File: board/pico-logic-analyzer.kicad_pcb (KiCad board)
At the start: 4 copper layers, 85 x 57.5 mm, 67 parts, among them J1 Conn_02x03_Odd_Even, J10 Conn_02x03_Odd_Even, J11 Conn_01x01, J2 Conn_02x03_Odd_Even, J3 Conn_02x03_Odd_Even, J4 Conn_02x03_Odd_Even, J5 Conn_02x03_Odd_Even, J6 Conn_02x03_Odd_Even, J7 Conn_02x03_Odd_Even, J8 Conn_02x03_Odd_Even, J9 Conn_02x03_Odd_Even, SW1 SW_Push, SW2 SW_DIP_x04, SW3 SW_DIP_x04, SW4 SW_DIP_x04, U1 LM2665M6, U2 LM4040DBZ-5, U3 TXB0104PW (fit with U104), U4 TXB0104PW (fit with U104), U5 TXB0104PW (fit with U104)

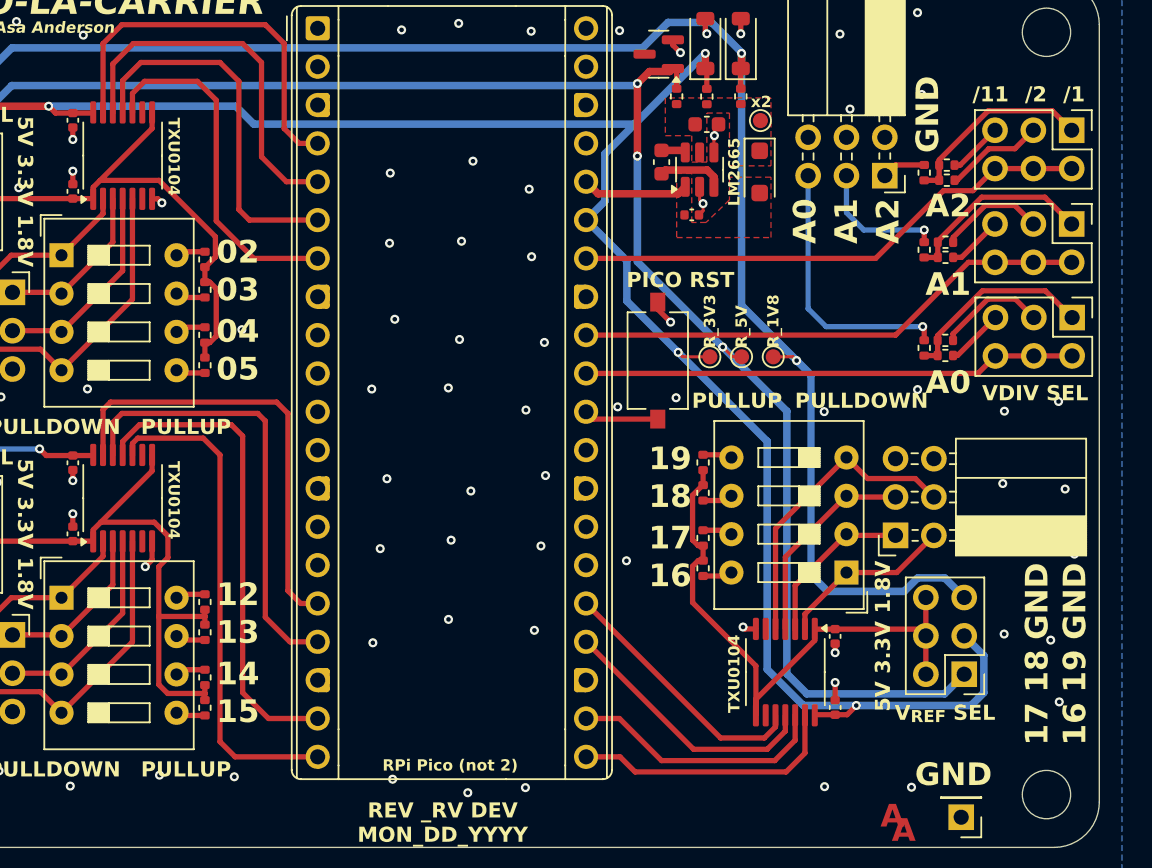
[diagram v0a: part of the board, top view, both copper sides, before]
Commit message: 2.0 first commit * started switching caps to standard value of 0603 4.7uF (which is overkill everywhere) * tidied up some silkscreen * replaced 4x100kOhm pullup resistors with 1 array (of the same values) * made some space for the zener clamping circuit (will still be a very tight fit)
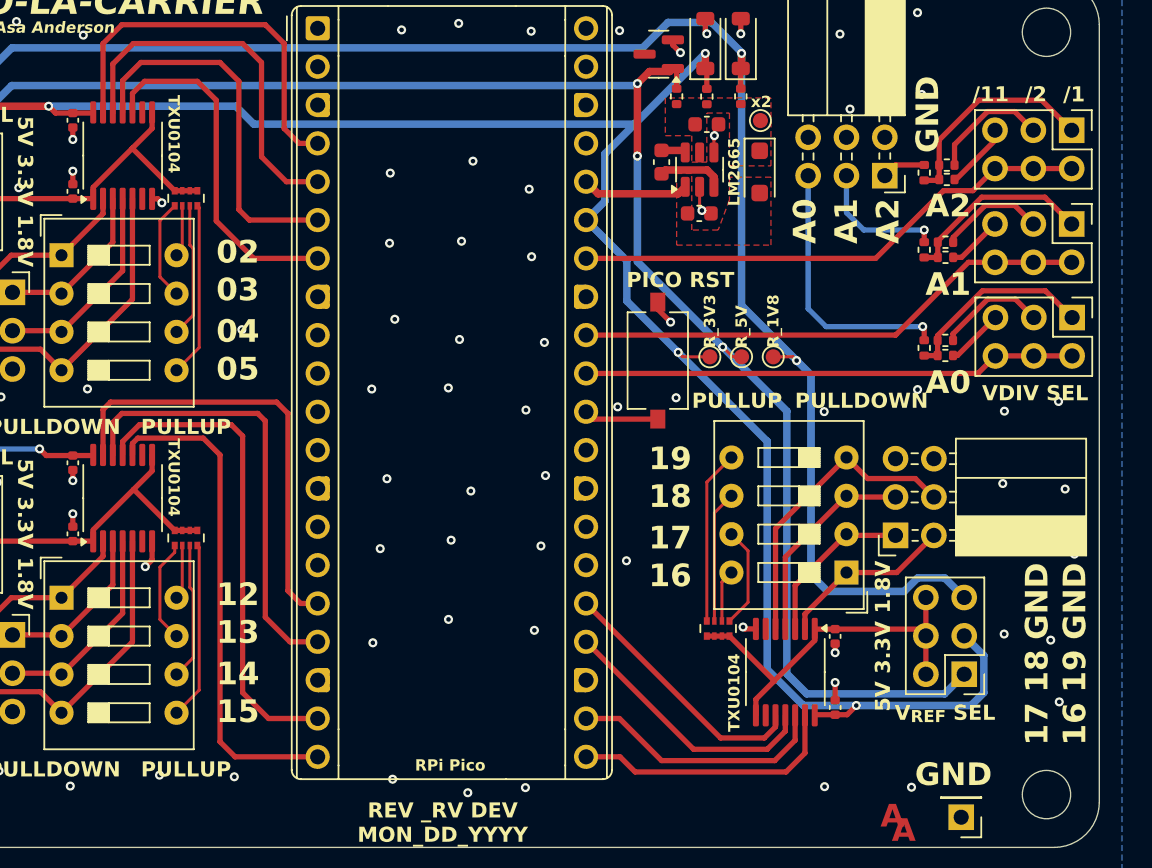
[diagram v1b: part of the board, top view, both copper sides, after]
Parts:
- removed R10, R11, R12, R13, R14, R15, R4, R5, R6, R7, R8, R9: 100k, Resistor_SMD:R_0402_1005Metric
- added RN1: 100k, Resistor_SMD:R_Array_Convex_4x0402, F.Cu at (150.5, 89.0)
- added RN2: 100k, Resistor_SMD:R_Array_Convex_4x0402, F.Cu at (150.5, 66.5)
- added RN3: 100k, Resistor_SMD:R_Array_Convex_4x0402, F.Cu at (185.8, 95.0)
- C1: value 1 uF -> 4.7 uF; footprint Capacitor_SMD:C_0402_1005Metric -> Capacitor_SMD:C_0603_1608Metric
- moved R17 1.00 mm to (200.9, 64.3)
- moved R18 0.95 mm to (200.9, 65.2)
- moved C1 0.51 mm to (184.5, 67.5)
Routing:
- net /Buffer Block A/VCCA_SEL: track 42.6 -> 24.7 mm
- net /Buffer Block C/VCCA_SEL: track 38.5 -> 25.0 mm
- net /Buffer Block B/VCCA_SEL: track 37.8 -> 24.8 mm
- net Net-(RN1D-R4.1): track 1.70 -> 11.8 mm
- net Net-(RN2D-R4.1): track 1.70 -> 11.6 mm
- net Net-(RN3D-R4.1): track 1.70 -> 11.5 mm
- net Net-(RN1C-R3.1): track 1.57 -> 9.09 mm
- net Net-(RN2C-R3.1): track 1.57 -> 8.90 mm
- net Net-(RN3C-R3.1): track 1.57 -> 8.76 mm
- net Net-(RN1A-R1.1): track 1.62 -> 6.86 mm
- net Net-(RN3A-R1.1): track 1.62 -> 6.72 mm
- net Net-(RN2A-R1.1): track 1.62 -> 6.67 mm
- net Net-(RN1B-R2.1): track 1.65 -> 3.62 mm
- net Net-(RN3B-R2.1): track 1.65 -> 3.47 mm
- net Net-(RN2B-R2.1): track 1.65 -> 3.43 mm
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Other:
- board text added: "RPi Pico"
- board text removed: "RPi Pico (not 2)"

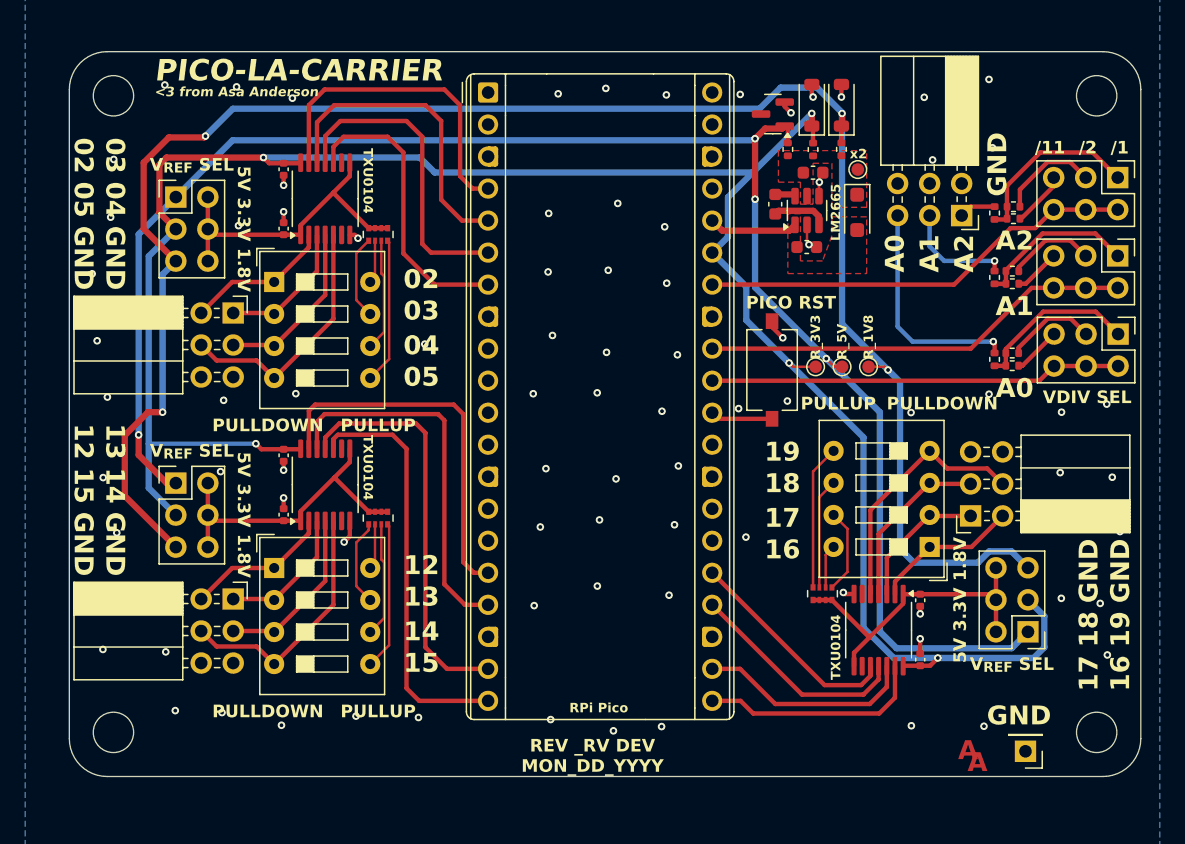
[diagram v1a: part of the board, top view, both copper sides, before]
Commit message: add zener diode clamping circuit
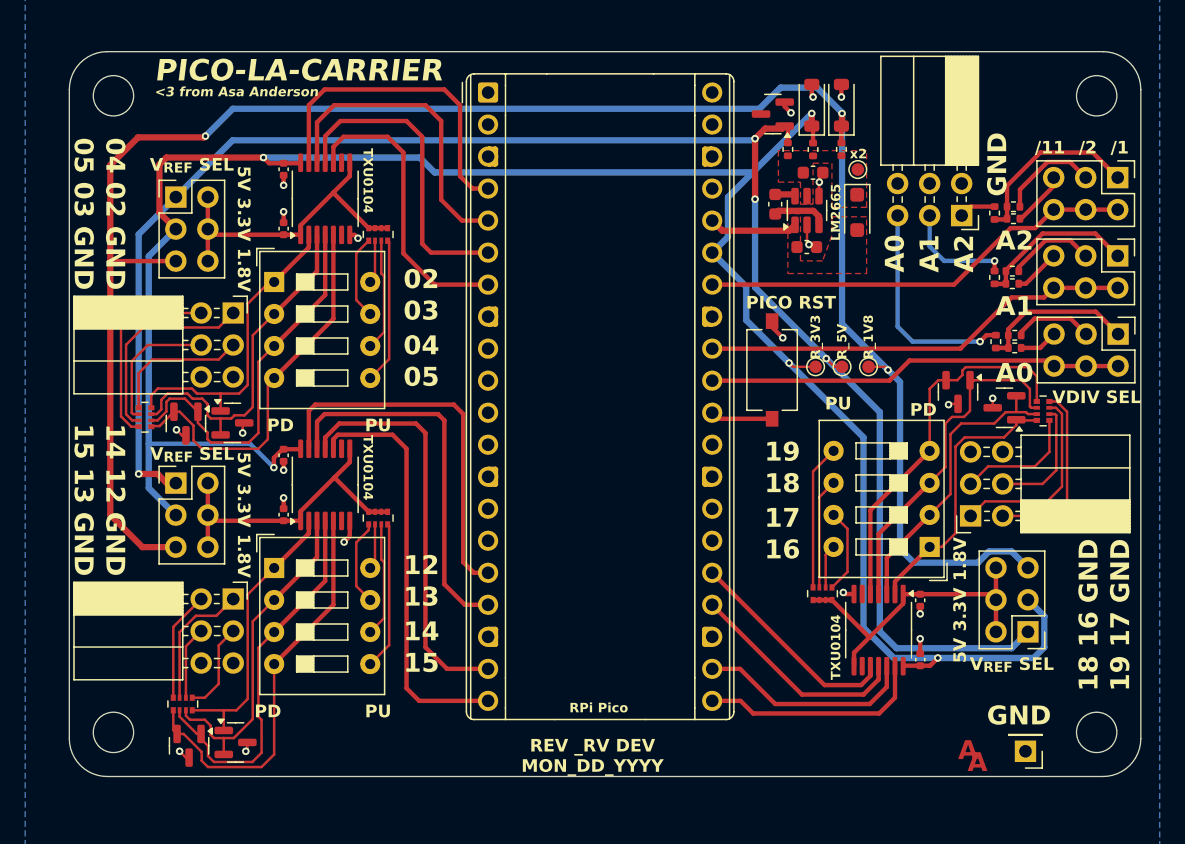
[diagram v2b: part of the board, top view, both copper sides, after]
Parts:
- added D4: 6.2 V_{z}, prefer better tolerances, Package_TO_SOT_SMD:SOT-23, F.Cu at (135.5, 107.1)
- added D5: 6.2 V_{z}, prefer better tolerances, Package_TO_SOT_SMD:SOT-23, F.Cu at (135.2, 81.5)
- added D6: 6.2 V_{z}, prefer better tolerances, Package_TO_SOT_SMD:SOT-23, F.Cu at (196.5, 79.0)
- added D7: 6.2 V_{z}, prefer better tolerances, Package_TO_SOT_SMD:SOT-23, F.Cu at (139.2, 106.8)
- added D8: 6.2 V_{z}, prefer better tolerances, Package_TO_SOT_SMD:SOT-23, F.Cu at (138.9, 81.5)
- added D9: 6.2 V_{z}, prefer better tolerances, Package_TO_SOT_SMD:SOT-23, F.Cu at (200.2, 80.2)
- added RN4: 470, Resistor_SMD:R_Array_Convex_4x0402, F.Cu at (135.0, 103.8)
- added RN5: 470, Resistor_SMD:R_Array_Convex_4x0402, F.Cu at (132.0, 81.0)
- added RN6: 470, Resistor_SMD:R_Array_Convex_4x0402, F.Cu at (203.2, 80.5)
- moved R23 1.42 mm to (201.0, 74.5)
- moved R24 1.42 mm to (201.0, 75.5)
- moved R22 1.41 mm to (199.5, 75.0)
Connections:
- J3 pad 1: /Buffer Block A/A1 -> /Buffer Block A/A2
- J3 pad 2: /Buffer Block A/A0 -> /Buffer Block A/A3
- J3 pad 3: /Buffer Block A/A2 -> /Buffer Block A/A0
- J3 pad 4: /Buffer Block A/A3 -> /Buffer Block A/A1
- J5 pad 1: /Buffer Block B/A1 -> /Buffer Block B/A2
- J5 pad 2: /Buffer Block B/A0 -> /Buffer Block B/A3
- J5 pad 3: /Buffer Block B/A2 -> /Buffer Block B/A0
- J5 pad 4: /Buffer Block B/A3 -> /Buffer Block B/A1
- J7 pad 1: /Buffer Block C/A1 -> /Buffer Block C/A2
- J7 pad 2: /Buffer Block C/A0 -> /Buffer Block C/A3
- J7 pad 3: /Buffer Block C/A2 -> /Buffer Block C/A0
- J7 pad 4: /Buffer Block C/A3 -> /Buffer Block C/A1
- SW2 pad 1: /Buffer Block A/A0 -> /Buffer Block A/A0_{CL}
- SW2 pad 2: /Buffer Block A/A1 -> /Buffer Block A/A1_{CL}
- SW2 pad 3: /Buffer Block A/A2 -> /Buffer Block A/A2_{CL}
- SW2 pad 4: /Buffer Block A/A3 -> /Buffer Block A/A3_{CL}
- SW3 pad 1: /Buffer Block B/A0 -> /Buffer Block B/A0_{CL}
- SW3 pad 2: /Buffer Block B/A1 -> /Buffer Block B/A1_{CL}
- SW3 pad 3: /Buffer Block B/A2 -> /Buffer Block B/A2_{CL}
- SW3 pad 4: /Buffer Block B/A3 -> /Buffer Block B/A3_{CL}
- SW4 pad 1: /Buffer Block C/A0 -> /Buffer Block C/A0_{CL}
- SW4 pad 2: /Buffer Block C/A1 -> /Buffer Block C/A1_{CL}
- SW4 pad 3: /Buffer Block C/A2 -> /Buffer Block C/A2_{CL}
- SW4 pad 4: /Buffer Block C/A3 -> /Buffer Block C/A3_{CL}
- U3 pad 2: /Buffer Block A/A0 -> /Buffer Block A/A0_{CL}
- U3 pad 3: /Buffer Block A/A1 -> /Buffer Block A/A1_{CL}
- U3 pad 4: /Buffer Block A/A2 -> /Buffer Block A/A2_{CL}
- U3 pad 5: /Buffer Block A/A3 -> /Buffer Block A/A3_{CL}
- U4 pad 2: /Buffer Block B/A0 -> /Buffer Block B/A0_{CL}
- U4 pad 3: /Buffer Block B/A1 -> /Buffer Block B/A1_{CL}
- U4 pad 4: /Buffer Block B/A2 -> /Buffer Block B/A2_{CL}
- U4 pad 5: /Buffer Block B/A3 -> /Buffer Block B/A3_{CL}
- U5 pad 2: /Buffer Block C/A0 -> /Buffer Block C/A0_{CL}
- U5 pad 3: /Buffer Block C/A1 -> /Buffer Block C/A1_{CL}
- U5 pad 4: /Buffer Block C/A2 -> /Buffer Block C/A2_{CL}
- U5 pad 5: /Buffer Block C/A3 -> /Buffer Block C/A3_{CL}
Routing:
- net /Buffer Block A/A3_{CL}: track 0.00 -> 32.1 mm
- net /Buffer Block B/A3_{CL}: track 0.00 -> 30.3 mm
- net /Buffer Block B/A2_{CL}: track 0.00 -> 30.2 mm
- net /Buffer Block C/A3_{CL}: track 0.00 -> 30.0 mm
- net /Buffer Block A/A2_{CL}: track 0.00 -> 29.8 mm
- net /Buffer Block B/A1_{CL}: track 0.00 -> 28.0 mm
- net /Buffer Block C/A2_{CL}: track 0.00 -> 27.7 mm
- net /Buffer Block A/A1_{CL}: track 0.00 -> 26.7 mm
- net /Buffer Block B/A0_{CL}: track 0.00 -> 24.5 mm
- net /Buffer Block C/A1_{CL}: track 0.00 -> 23.6 mm
- net /Buffer Block A/A0_{CL}: track 0.00 -> 22.5 mm
- net /Buffer Block C/A0_{CL}: track 0.00 -> 21.8 mm
- net /Buffer Block A/A3: track 20.2 -> 8.75 mm
- net /+1.8V_REG: track 146.2 -> 152.7 mm, vias 4 -> 3
- net /Buffer Block C/A3: track 20.2 -> 14.4 mm
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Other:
- board text added: "PD"
- board text added: "PU"
- board text removed: "PULLDOWN"
- board text removed: "PULLUP"

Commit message: remove 3.3v zener from sch - start to switch to stdlib rpi pico -
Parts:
- removed D3: 3.3v, Diode_SMD:D_SOD-123
- removed R2: 270, >1/10 W, Resistor_SMD:R_0402_1005Metric
- removed TP1, TP2, TP3: TestPoint, TestPoint:TestPoint_Pad_D1.0mm
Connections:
- A1 pad 35: /+3.3V_REG -> unconnected-(A1-ADC_VREF-Pad35)
- C5 pad 2: /+3.3V_REG -> +3V3
- C7 pad 2: /+3.3V_REG -> +3V3
- C9 pad 2: /+3.3V_REG -> +3V3
- J2 pad 3: /+3.3V_REG -> +3V3
- J4 pad 3: /+3.3V_REG -> +3V3
- J6 pad 3: /+3.3V_REG -> +3V3
- U3 pad 14: /+3.3V_REG -> +3V3
- U4 pad 14: /+3.3V_REG -> +3V3
- U5 pad 14: /+3.3V_REG -> +3V3
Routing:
- net /+3.3V_REG: track 171.5 -> 0.00 mm, vias 5 -> 0
- net +3V3: track 7.09 -> 35.7 mm
- net /+1.8V_REG: track 152.7 -> 151.0 mm, vias 3 -> 2
- net /+5V_REG: track 136.1 -> 134.6 mm, vias 4 -> 3
- net GND: track 22.0 -> 21.0 mm, vias 21 -> 20
